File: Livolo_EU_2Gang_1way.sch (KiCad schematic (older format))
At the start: 39 parts, among them IC1 ATMEGA328P, U1 ATSHA204A, U2 RFM69_MINIMAL

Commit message: cleanup schema
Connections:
- net N$1: no longer names the net of D6.2 (A), R1.1
- net N$10: no longer names the net of D4.1 (K), R8.1
- net N$14: no longer names the net of U$7.P$1 (1), U2.ANT
- net N$2: no longer names the net of IC1.7 (PB6(XTAL1/TOSC1)), U$3.1
- net N$3: no longer names the net of C4.2, U$1.SENS (SENSEPAD), U$4.3 (IN)
- net N$4: no longer names the net of C2.2, IC1.20 (AREF)
- net N$5: no longer names the net of D1.2 (A), R5.2
- net N$6: no longer names the net of D2.1 (K), R6.1
- net N$7: no longer names the net of D3.2 (A), R7.2
- net N$8: no longer names the net of IC1.8 (PB7(XTAL2/TOSC2)), U$3.3
- net N$9: no longer names the net of C8.2, U$5.SENS (SENSEPAD), U$6.3 (IN)
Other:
- moved on the sheet: C4, C8, R10, U$8

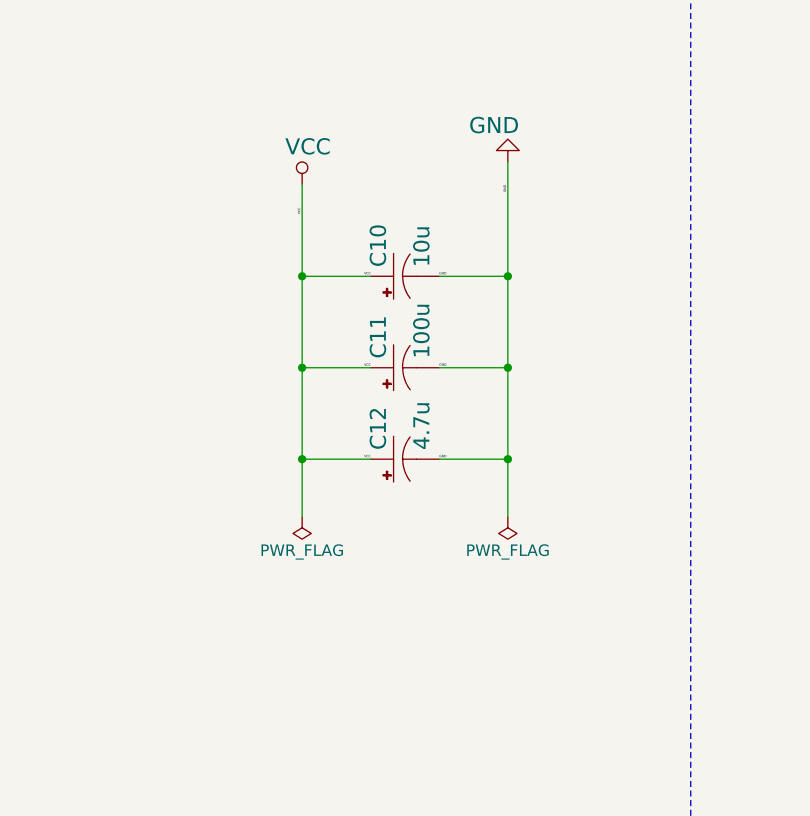
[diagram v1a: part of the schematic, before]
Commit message: Ceramic capacitor added in parrallel of Tantalum
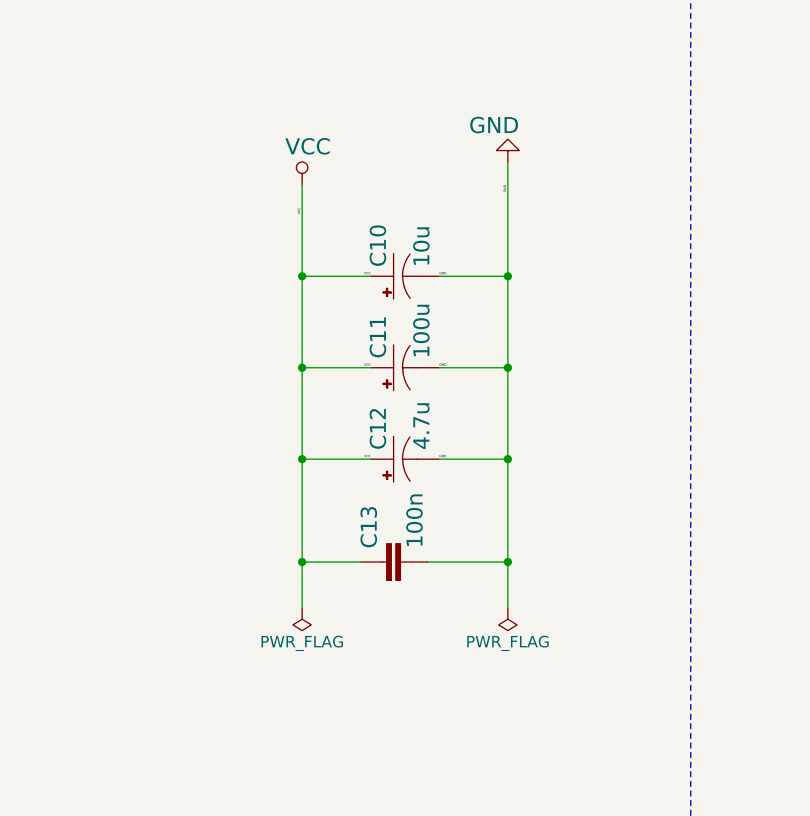
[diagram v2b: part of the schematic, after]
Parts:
- added C13: 100n, Capacitors_SMD:C_0805_HandSoldering, symbol CAP0402-CAP
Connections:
- net GND: now also C13.2
- net VCC: now also C13.1
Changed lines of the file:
@@
 L PWR_FLAG #FLG026
 U 1 1 58E02AA4
-P 1850 3500
-F 0 "#FLG026" H 1850 3575 50  0001 C CNN
-F 1 "PWR_FLAG" H 1850 3650 50  0000 C CNN
-F 2 "" H 1850 3500 50  0001 C CNN
-F 3 "" H 1850 3500 50  0001 C CNN
-	1    1850 3500
+P 1850 3900
+F 0 "#FLG026" H 1850 3975 50  0001 C CNN
+F 1 "PWR_FLAG" H 1850 4050 50  0000 C CNN
+F 2 "" H 1850 3900 50  0001 C CNN
+F 3 "" H 1850 3900 50  0001 C CNN
+	1    1850 3900
 	-1   0    0    1
 $EndComp
@@
 L PWR_FLAG #FLG027
 U 1 1 58E02B1B
-P 2750 3500
-F 0 "#FLG027" H 2750 3575 50  0001 C CNN
-F 1 "PWR_FLAG" H 2750 3650 50  0000 C CNN
-F 2 "" H 2750 3500 50  0001 C CNN
-F 3 "" H 2750 3500 50  0001 C CNN
-	1    2750 3500
+P 2750 3900
+F 0 "#FLG027" H 2750 3975 50  0001 C CNN
+F 1 "PWR_FLAG" H 2750 4050 50  0000 C CNN
+F 2 "" H 2750 3900 50  0001 C CNN
+F 3 "" H 2750 3900 50  0001 C CNN
+	1    2750 3900
 	-1   0    0    1
 $EndComp
@@
 Connection ~ 2750 3250
 Wire Wire Line
-	1850 2050 1850 3500
-Wire Wire Line
-	2750 1950 2750 3500
+	1850 2050 1850 3900
+Wire Wire Line
+	2750 1950 2750 3900
 Wire Wire Line
 	13500 7750 13650 7750
@@
 Wire Notes Line
 	3550 8300 500  8300
+Connection ~ 2750 3700
+Connection ~ 1850 3700
+Wire Wire Line
+	2400 3700 2750 3700
+Wire Wire Line
+	2100 3700 1850 3700
+$Comp
+L CAP0402-CAP C13
+U 1 1 58E25150
+P 2300 3700
+F 0 "C13" H 2359 3815 70  0000 L BNN
+F 1 "100n" H 2360 3615 70  0000 L BNN
+F 2 "Capacitors_SMD:C_0805_HandSoldering" H 2290 3490 65  0001 L TNN
+F 3 "" H 2300 3700 60  0001 C CNN
+	1    2300 3700
+	0    -1   -1   0
+$EndComp
 $EndSCHEMATC

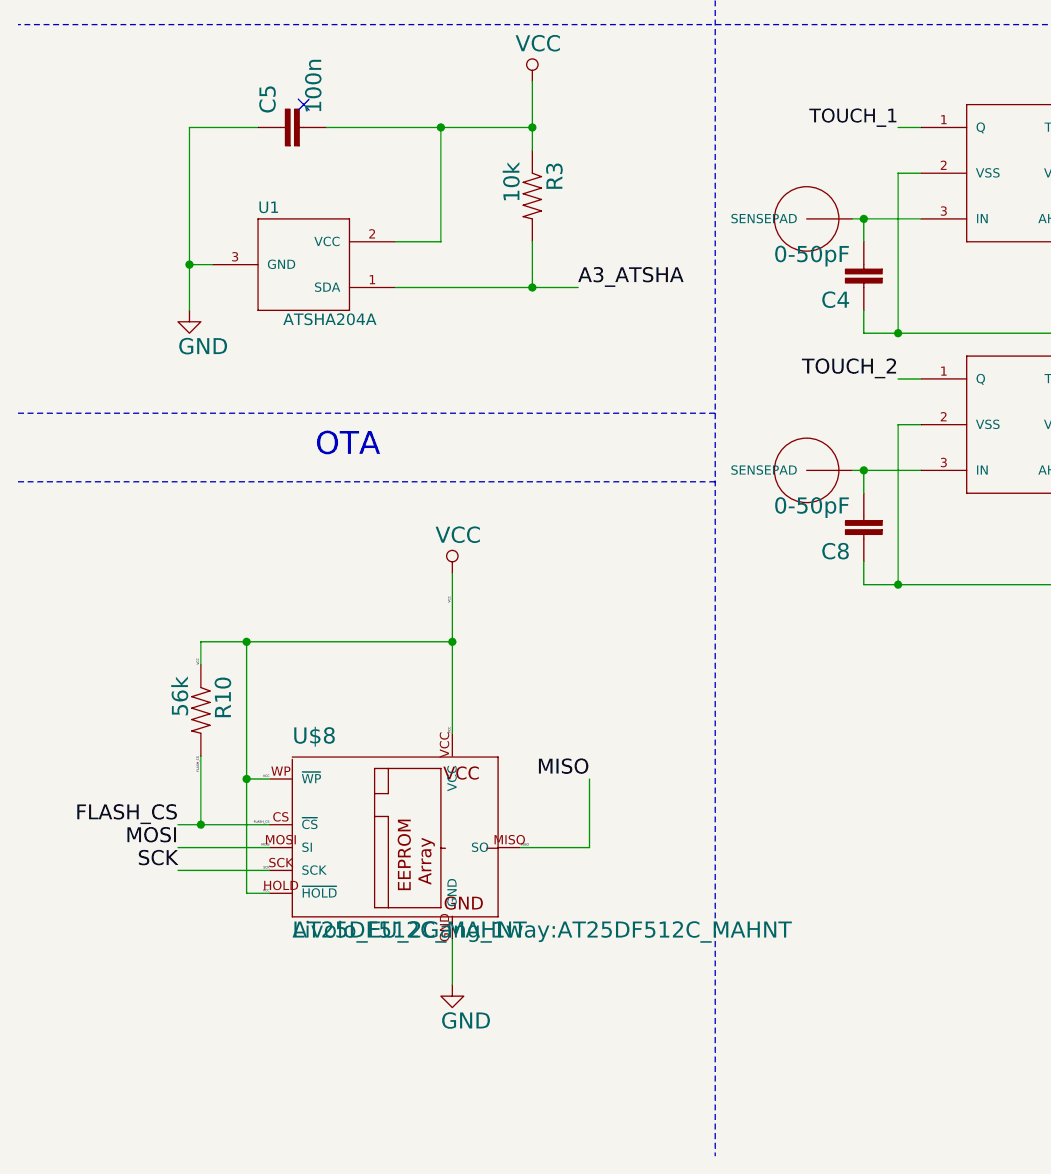
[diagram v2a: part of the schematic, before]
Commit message: capacitor added for OTA
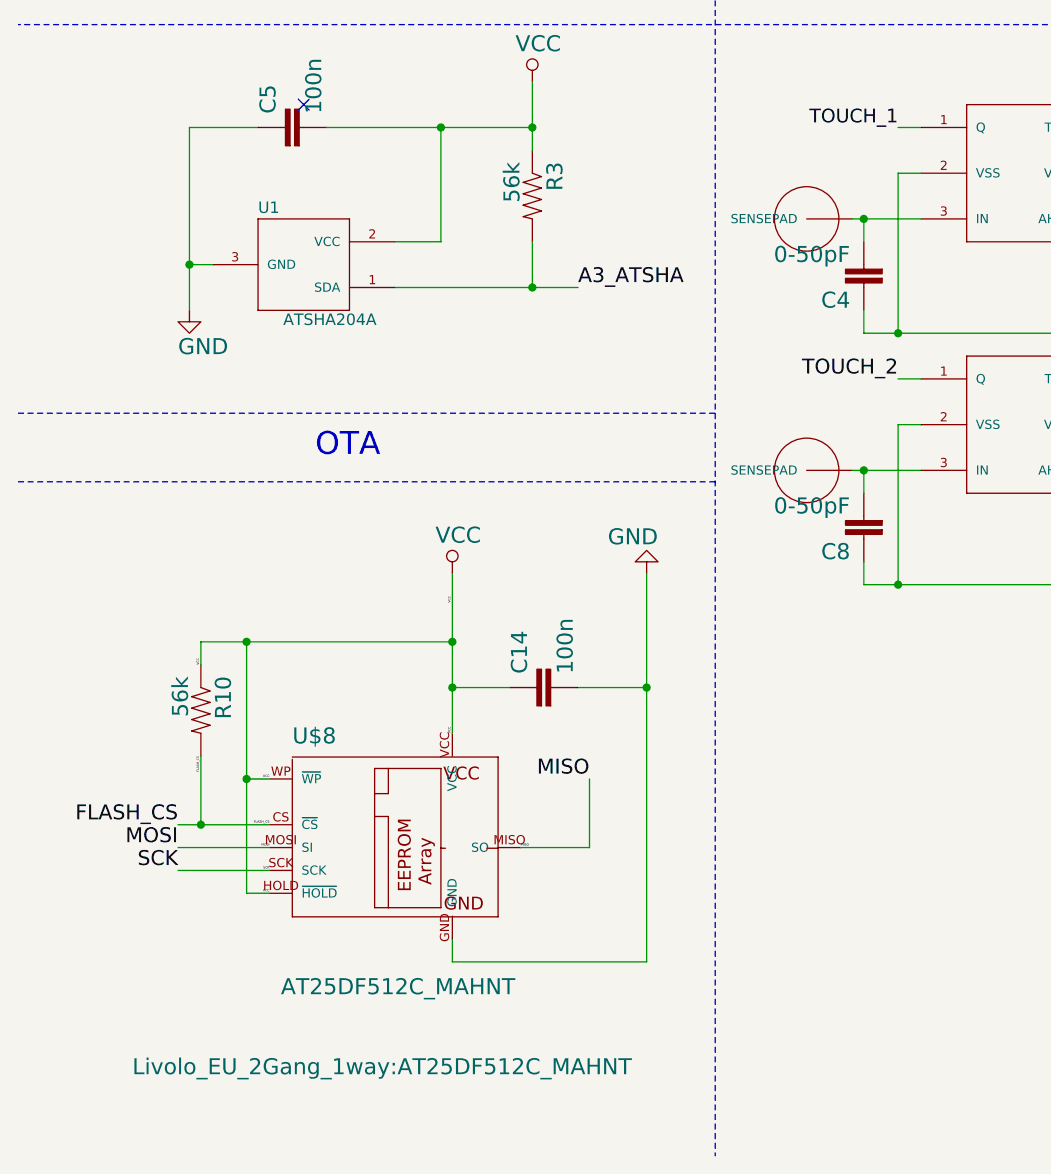
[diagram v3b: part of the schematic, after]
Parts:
- added C14: 100n, Capacitors_SMD:C_0603_HandSoldering, symbol CAP0603-CAP
- C2: footprint Capacitors_SMD:C_0402 -> Capacitors_SMD:C_0603_HandSoldering
- R3: value 10k -> 56k
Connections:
- net GND: now also C14.2
- net VCC: now also C14.1
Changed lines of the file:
@@
 F 0 "C2" H 6309 3465 70  0000 L BNN
 F 1 "100n" H 6310 3265 70  0000 L BNN
-F 2 "Capacitors_SMD:C_0402" H 6240 3140 65  0001 L TNN
+F 2 "Capacitors_SMD:C_0603_HandSoldering" H 6240 3140 65  0001 L TNN
 F 3 "" H 6250 3350 60  0001 C CNN
 	1    6250 3350
@@
 P 2750 7050
 F 0 "R3" H 2600 7108 70  0000 L BNN
-F 1 "10k" H 2601 6920 70  0000 L BNN
+F 1 "56k" H 2601 6920 70  0000 L BNN
 F 2 "Resistors_SMD:R_0603_HandSoldering" H 2740 6840 65  0001 L TNN
 F 3 "" H 2750 7050 60  0001 C CNN
@@
 P 2200 9900
 F 0 "U$8" H 1700 10347 70  0000 L BNN
-F 1 "AT25DF512C_MAHNT" H 1700 9498 70  0000 L BNN
-F 2 "Livolo_EU_2Gang_1way:AT25DF512C_MAHNT" H 1700 9498 70  0000 L BNN
+F 1 "AT25DF512C_MAHNT" H 1650 9250 70  0000 L BNN
+F 2 "Livolo_EU_2Gang_1way:AT25DF512C_MAHNT" H 1000 8900 70  0000 L BNN
 F 3 "" H 2200 9900 60  0001 C CNN
 	1    2200 9900
@@
 NoConn ~ 1750 6650
 $Comp
-L GND #GND025
-U 1 1 58DFE7F7
-P 2400 10500
-F 0 "#GND025" H 2300 10400 70  0001 L BNN
-F 1 "GND" H 2350 10300 70  0000 L BNN
-F 2 "" H 2400 10500 60  0001 C CNN
-F 3 "" H 2400 10500 60  0001 C CNN
-	1    2400 10500
-	1    0    0    -1
-$EndComp
-$Comp
-L PWR_FLAG #FLG026
+L PWR_FLAG #FLG025
 U 1 1 58E02AA4
 P 1850 3900
-F 0 "#FLG026" H 1850 3975 50  0001 C CNN
+F 0 "#FLG025" H 1850 3975 50  0001 C CNN
 F 1 "PWR_FLAG" H 1850 4050 50  0000 C CNN
 F 2 "" H 1850 3900 50  0001 C CNN
@@
 $EndComp
 $Comp
-L PWR_FLAG #FLG027
+L PWR_FLAG #FLG026
 U 1 1 58E02B1B
 P 2750 3900
-F 0 "#FLG027" H 2750 3975 50  0001 C CNN
+F 0 "#FLG026" H 2750 3975 50  0001 C CNN
 F 1 "PWR_FLAG" H 2750 4050 50  0000 C CNN
 F 2 "" H 2750 3900 50  0001 C CNN
@@
 Wire Wire Line
 	13500 7750 13650 7750
-Wire Wire Line
-	2400 10300 2400 10500
 Wire Bus Line
 	9350 8500 9450 8850
@@
 	0    -1   -1   0
 $EndComp
+$Comp
+L GND #GND027
+U 1 1 58E32C86
+P 3250 8700
+F 0 "#GND027" H 3150 8600 70  0001 L BNN
+F 1 "GND" H 3200 8500 70  0000 L BNN
+F 2 "" H 3250 8700 60  0001 C CNN
+F 3 "" H 3250 8700 60  0001 C CNN
+	1    3250 8700
+	-1   0    0    1
+$EndComp
+$Comp
+L CAP0603-CAP C14
+U 1 1 58E32EE4
+P 2850 9200
+F 0 "C14" H 2910 9315 70  0000 L BNN
+F 1 "100n" H 2910 9115 70  0000 L BNN
+F 2 "Capacitors_SMD:C_0603_HandSoldering" H 2840 8990 65  0001 L TNN
+F 3 "" H 2850 9200 60  0001 C CNN
+	1    2850 9200
+	0    -1   -1   0
+$EndComp
+Wire Wire Line
+	3250 8700 3250 10400
+Wire Wire Line
+	2950 9200 3250 9200
+Wire Wire Line
+	2400 9200 2650 9200
+Connection ~ 2400 9200
+Wire Wire Line
+	3250 10400 2400 10400
+Connection ~ 3250 9200
+Wire Wire Line
+	2400 10400 2400 10300
 $EndSCHEMATC

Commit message: Text cleaning and Readme update
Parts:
- U$7: value RFM12B_ANTENNA -> ANT
- U2: value RFM69_MINIMAL -> RFM69CW
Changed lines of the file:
@@
 P 15350 3750
 F 0 "U$7" H 15340 3740 65  0001 L TNN
-F 1 "RFM12B_ANTENNA" H 15340 3640 65  0001 L TNN
+F 1 "ANT" H 15340 3640 65  0001 L TNN
 F 2 "Livolo_EU_2Gang_1way:RFM12B-ANTENNA" H 15340 3540 65  0001 L TNN
 F 3 "" H 15350 3750 60  0001 C CNN
@@
 P 14550 3850
 F 0 "U2" H 14151 4450 50  0000 L BNN
-F 1 "RFM69_MINIMAL" H 14150 3250 50  0000 L BNN
+F 1 "RFM69CW" H 14150 3250 50  0000 L BNN
 F 2 "Livolo_EU_2Gang_1way:RFM69CW_MINIMAL" H 14540 3640 65  0001 L TNN
 F 3 "" H 14550 3850 60  0001 C CNN
